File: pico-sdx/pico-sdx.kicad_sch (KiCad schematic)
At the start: 5 parts, among them J1 AudioJack3, J2 AudioJack3, J3 Screw_Terminal_01x02, J4 Conn_Coaxial, J5 Conn_Coaxial

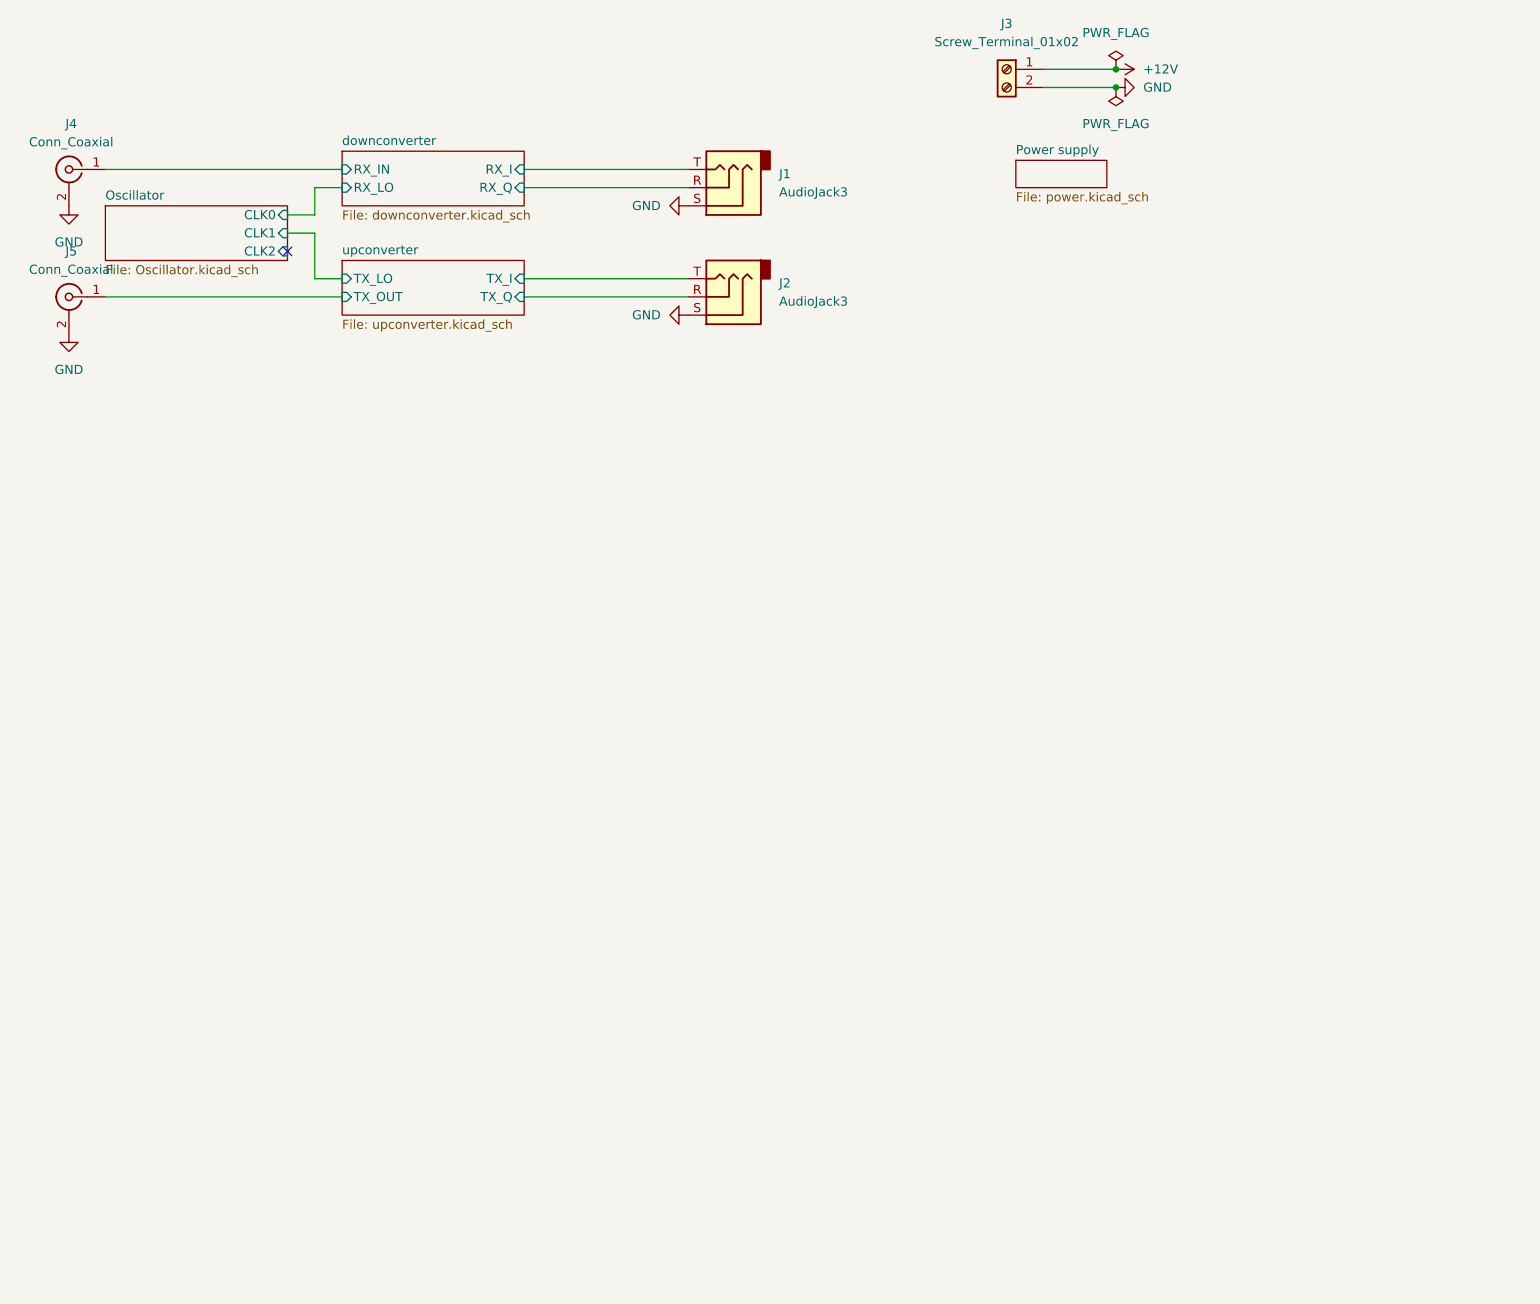
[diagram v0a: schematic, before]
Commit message: add documentation and RaspberryPi Pico
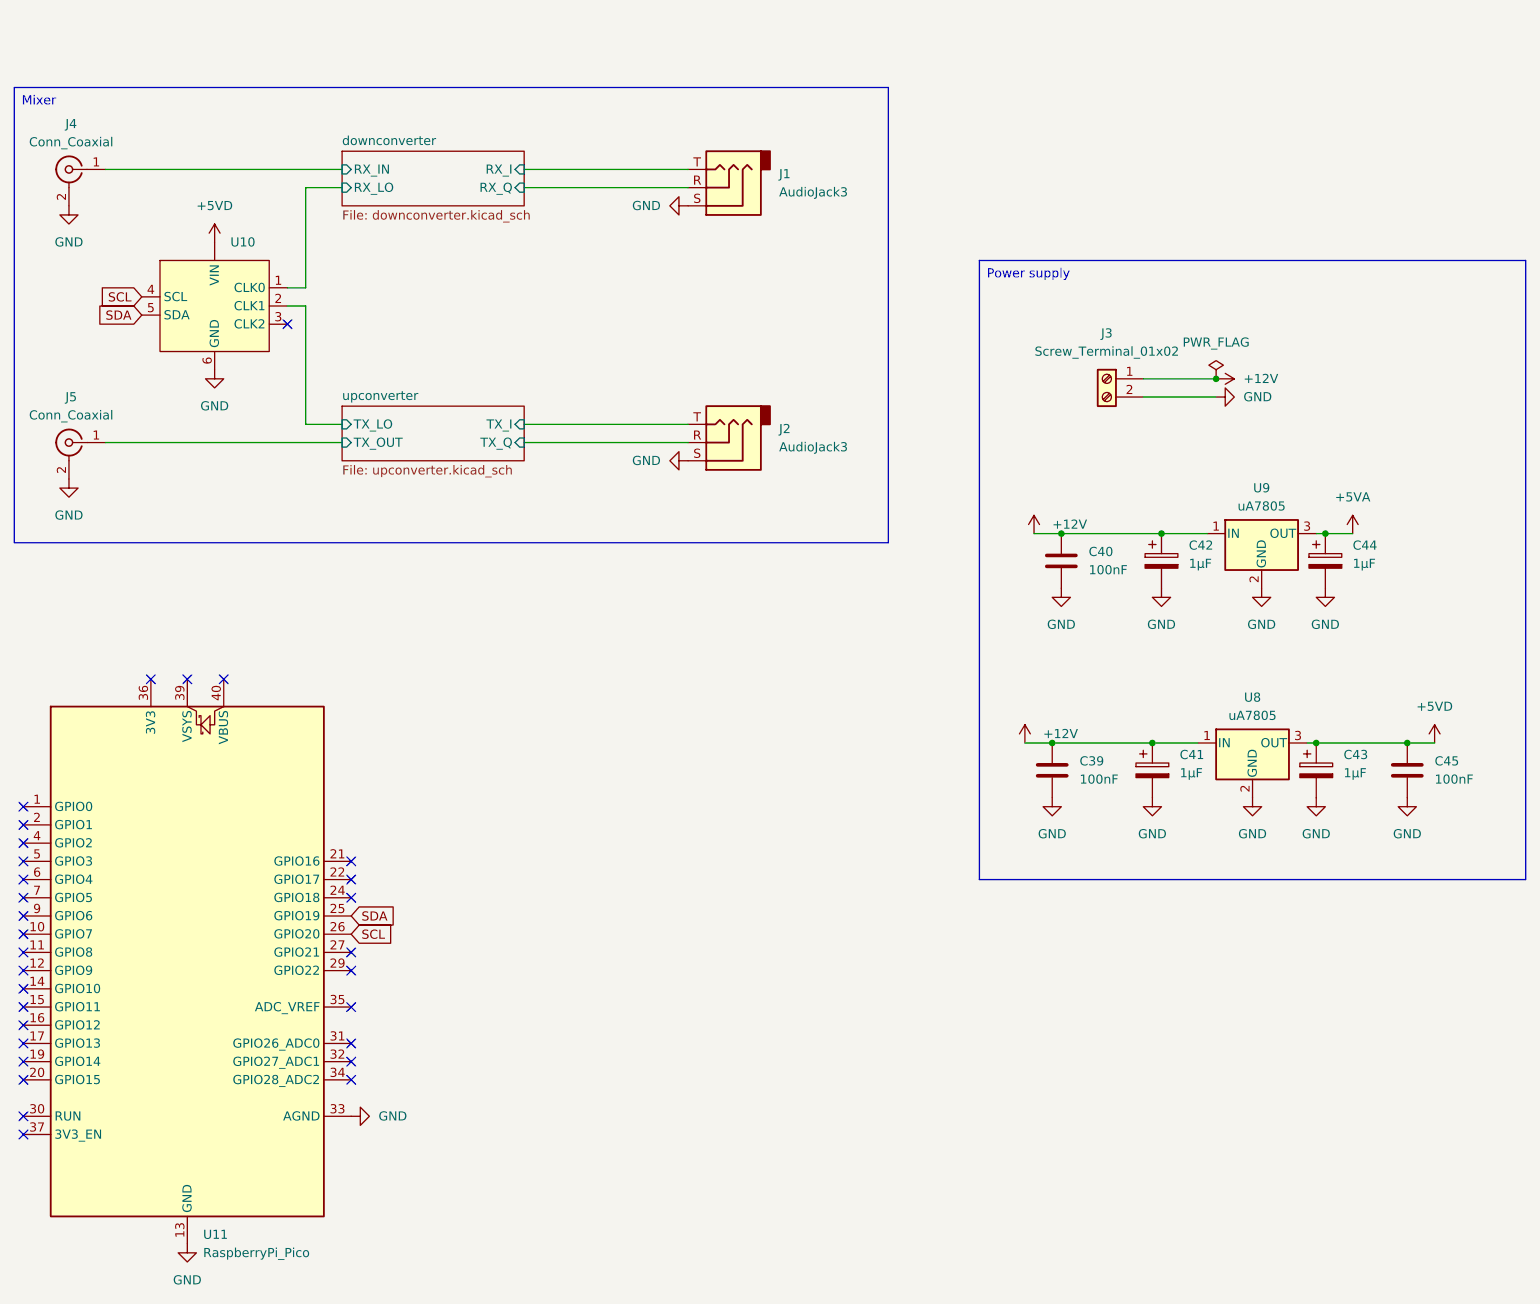
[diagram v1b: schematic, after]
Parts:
- added C39, C40, C45: 100nF, Capacitor_SMD:C_0603_1608Metric, symbol Device:C
- added C41, C42, C43, C44: 1µF, Capacitor_Tantalum_SMD:CP_EIA-3216-18_Kemet-A, symbol Device:C_Polarized
- added U10: ~, pico-sdx:Module_Si5351, symbol pico-sdx:Si5351A_Clock_Generator_Breakout_
- added U11: RaspberryPi_Pico, Module_RaspberryPi_Pico:RaspberryPi_Pico_Common, symbol MCU_Module_RaspberryPi_Pico:RaspberryPi_Pico
- added U8, U9: uA7805, Package_TO_SOT_THT:TO-220-3_Vertical, symbol Regulator_Linear:uA7805
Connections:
- net +12V: now also C39.1, C40.1, C41.1, C42.1, U8.1 (IN), U9.1 (IN)
- net GND: now also C39.2, C40.2, C41.2, C42.2, C43.2, C44.2, C45.2, U10.6 (GND), U11.13 (GND), U11.18 (GND), U11.23 (GND), U11.28 (GND), U11.3 (GND), U11.33 (AGND), U11.38 (GND), U11.8 (GND), U8.2 (GND), U9.2 (GND)
- new net +5VA: C44.1, U9.3 (OUT)
- new net +5VD: C43.1, C45.1, U10. (VIN), U8.3 (OUT)
- new net SCL: U10.4 (SCL), U11.26 (GPIO20)
- new net SDA: U10.5 (SDA), U11.25 (GPIO19)
- new net downconverter/RX_LO: U10.1 (CLK0)
- new net upconverter/TX_LO: U10.2 (CLK1)
- no-connect marks 1 -> 31
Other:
- removed sheet Oscillator
- removed sheet Power supply
- moved on the sheet: J2, J3, J5

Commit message: routed with filter relays without PA
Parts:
- removed J3: Screw_Terminal_01x02, TerminalBlock:TerminalBlock_Wuerth_691311400102_P7.62mm, symbol Connector:Screw_Terminal_01x02
- added D1, D2: D, Diode_SMD:D_SOD-128, symbol Device:D
- added J1: Antenna, Connector_Coaxial:SMA_Amphenol_132289_EdgeMount, symbol Connector:Conn_Coaxial
- added J2: RX, Connector_Coaxial:SMA_Amphenol_132289_EdgeMount, symbol Connector:Conn_Coaxial
- added J3: TX, Connector_Coaxial:SMA_Amphenol_132289_EdgeMount, symbol Connector:Conn_Coaxial
- added J8: Barrel_Jack_Switch, Connector_BarrelJack:BarrelJack_Wuerth_6941xx301002, symbol Connector:Barrel_Jack_Switch
- added K1, K2: G6K-2, Relay_THT:Relay_DPDT_Omron_G6K-2P, symbol Relay:G6K-2
- added TP1: RX_LO, TestPoint:TestPoint_Loop_D1.80mm_Drill1.0mm_Beaded, symbol Connector:TestPoint
- added TP2: TX_LO, TestPoint:TestPoint_Loop_D1.80mm_Drill1.0mm_Beaded, symbol Connector:TestPoint
- added U1: MAX4820xUP, Package_SO:HTSSOP-20-1EP_4.4x6.5mm_P0.65mm_EP2.85x4mm, symbol Driver_Relay:MAX4820xUP
- J4, J5: footprint Connector_Coaxial:SMA_Amphenol_132289_EdgeMount -> Connector_Coaxial:SMA_Amphenol_132291_Vertical
- renumbered C39 to C1, C40 to C2, C41 to C3, C42 to C4, C43 to C5, C44 to C6, C45 to C7, J1 to J6, J2 to J7, U11 to U2, U10 to U3, U8 to U4, U9 to U5
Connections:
- net Downconverter/RX_LO is gone; now on net +5VD: U3.1 (VIN)
- net Upconverter/TX_LO is gone; now on net GND: U3.2 (GND)
- net +12V: now also J8.1
- net +5VD: now also U2.39 (VSYS), U1.1 (VCC), U1.15 (COM), U1.2 (~{SET}); no longer U3. (VIN)
- net GND: now also D1.2 (A), D2.2 (A), J1.2 (Ext), J2.2 (Ext), J3.2 (Ext), J8.2, K1.8, K2.8, U1.12 (GND), U1.18 (GND), U1.21 (GND), U1.9 (GND); no longer U3.6 (GND)
- net SCL: now also U2.20 (GPIO15); no longer U2.26 (GPIO20)
- net SDA: now also U2.19 (GPIO14), U3.3 (SDA); no longer U2.25 (GPIO19), U3.5 (SDA)
- net Downconverter/RX_IN: now also K1.2
- net Upconverter/TX_OUT: now also K1.5
- net MISO: now reaches U2.21 (GPIO16)
- net MISO: now also U1.7 (DOUT)
- net ~{CS}: now reaches U2.22 (GPIO17)
- net ~{CS}: now also U1.4 (~{CS})
- net SCLK: now reaches U2.24 (GPIO18)
- net SCLK: now also U1.6 (SCLK)
- new net: J2.1 (In), K1.7, K2.2
- new net: J1.1 (In), K2.3
- new net 10 m: U1.20 (OUT1)
- new net 12 m: U1.19 (OUT2)
- new net 15 m: U1.17 (OUT3)
- new net 17 m: U1.16 (OUT4)
- new net 20 m: U1.14 (OUT5)
- new net 30 m: U1.13 (OUT6)
- new net 40 m: U1.11 (OUT7)
- new net Bandpass Filter/RF in: K1.6
- new net Buffer Amplifier/RF out: K1.3
- new net MOSI: U1.5 (DIN), U2.25 (GPIO19)
- new net PA/TX in: J3.1 (In), K1.4
- new net PA/TX out: K2.4
- new net RX_LO: TP1.1, U3.6 (CLK1)
- new net TX_LO: TP2.1, U3.7 (CLK0)
- new net TX~{RX}: D1.1 (K), D2.1 (K), K1.1, K2.1, U1.10 (OUT8)
- new net ~{RESET}: U1.3 (~{RESET}), U2.26 (GPIO20)
- no-connect marks 31 -> 29
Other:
- sheet downconverter renamed Downconverter
- sheet upconverter renamed Upconverter
- added sheet Bandpass Filter (bpf.kicad_sch)
- added sheet Buffer Amplifier (buffer.kicad_sch)
- added sheet PA (PA.kicad_sch)
- moved on the sheet: J4, J5

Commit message: modular design
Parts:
- removed D1, D2: D, Diode_SMD:D_SOD-128, symbol Device:D
- removed J1: Antenna, Connector_Coaxial:SMA_Amphenol_132289_EdgeMount, symbol Connector:Conn_Coaxial
- removed J2: RX, Connector_Coaxial:SMA_Amphenol_132289_EdgeMount, symbol Connector:Conn_Coaxial
- removed J3: TX, Connector_Coaxial:SMA_Amphenol_132289_EdgeMount, symbol Connector:Conn_Coaxial
- removed K1, K2: G6K-2, Relay_THT:Relay_DPDT_Omron_G6K-2P, symbol Relay:G6K-2
- removed TP1: RX_LO, TestPoint:TestPoint_Loop_D1.80mm_Drill1.0mm_Beaded, symbol Connector:TestPoint
- removed TP2: TX_LO, TestPoint:TestPoint_Loop_D1.80mm_Drill1.0mm_Beaded, symbol Connector:TestPoint
- removed U1: MAX4820xUP, Package_SO:HTSSOP-20-1EP_4.4x6.5mm_P0.65mm_EP2.85x4mm, symbol Driver_Relay:MAX4820xUP
- removed U2: RaspberryPi_Pico, Module_RaspberryPi_Pico:RaspberryPi_Pico_Common, symbol MCU_Module_RaspberryPi_Pico:RaspberryPi_Pico
- removed U3: ~, pico-sdx:Module_Si5351, symbol pico-sdx:Si5351A_Clock_Generator_Breakout_
- removed U4: uA7805, Package_TO_SOT_THT:TO-220-3_Vertical, symbol Regulator_Linear:uA7805
- added PMOD1: PMOD-Device-x2-Type-2A-Expanded-SPI, pmod-conn_6x2:pmod_pin_array_6x2, symbol pmod:PMOD-Device-x2-Type-2A-Expanded-SPI
- added U17: TLE4284 DV33, Package_TO_SOT_SMD:TO-252-3_TabPin2, symbol Regulator_Linear:AMS1117CD-3.3
- added U3: Si5351C-B-GU, Package_SO:QSOP-24_3.9x8.7mm_P0.635mm, symbol pico-sdx:Si5351C-B-GU
- added X8: TCXO-14, Oscillator:Oscillator_DIP-14, symbol Oscillator:TCXO-14
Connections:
- net +12V: now also U17.3 (VI)
- net GND: now also U17.1 (GND), U3.13 (OEB), U3.17 (GND), U3.19 (GND), U3.5 (GND), U3.8 (GND), X8.7 (GND)
- net RX_LO: now also U3.21 (CLK0)
- net SCL: now also U3.10 (SCL)
- net SDA: now also U3.22 (VDDOD)
- net TX_LO: now also U3.20 (CLK1)
- net +5VD renamed +3.3V
- net +3.3V: now also U17.2 (VO), U3.16 (VDDOB), U3.18 (VDDOA), U3.2 (VDDOC), U3.22 (VDDOD), U3.4 (VDD), X8.14 (Vcc)
- net Downconverter/RX_IN renamed Buffer Amplifier/RF in
- new net: U3.12 (CLKIN), X8.8 (OUT)
- no-connect marks 29 -> 10
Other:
- removed sheet Bandpass Filter
- removed sheet PA
- moved on the sheet: J4, J5

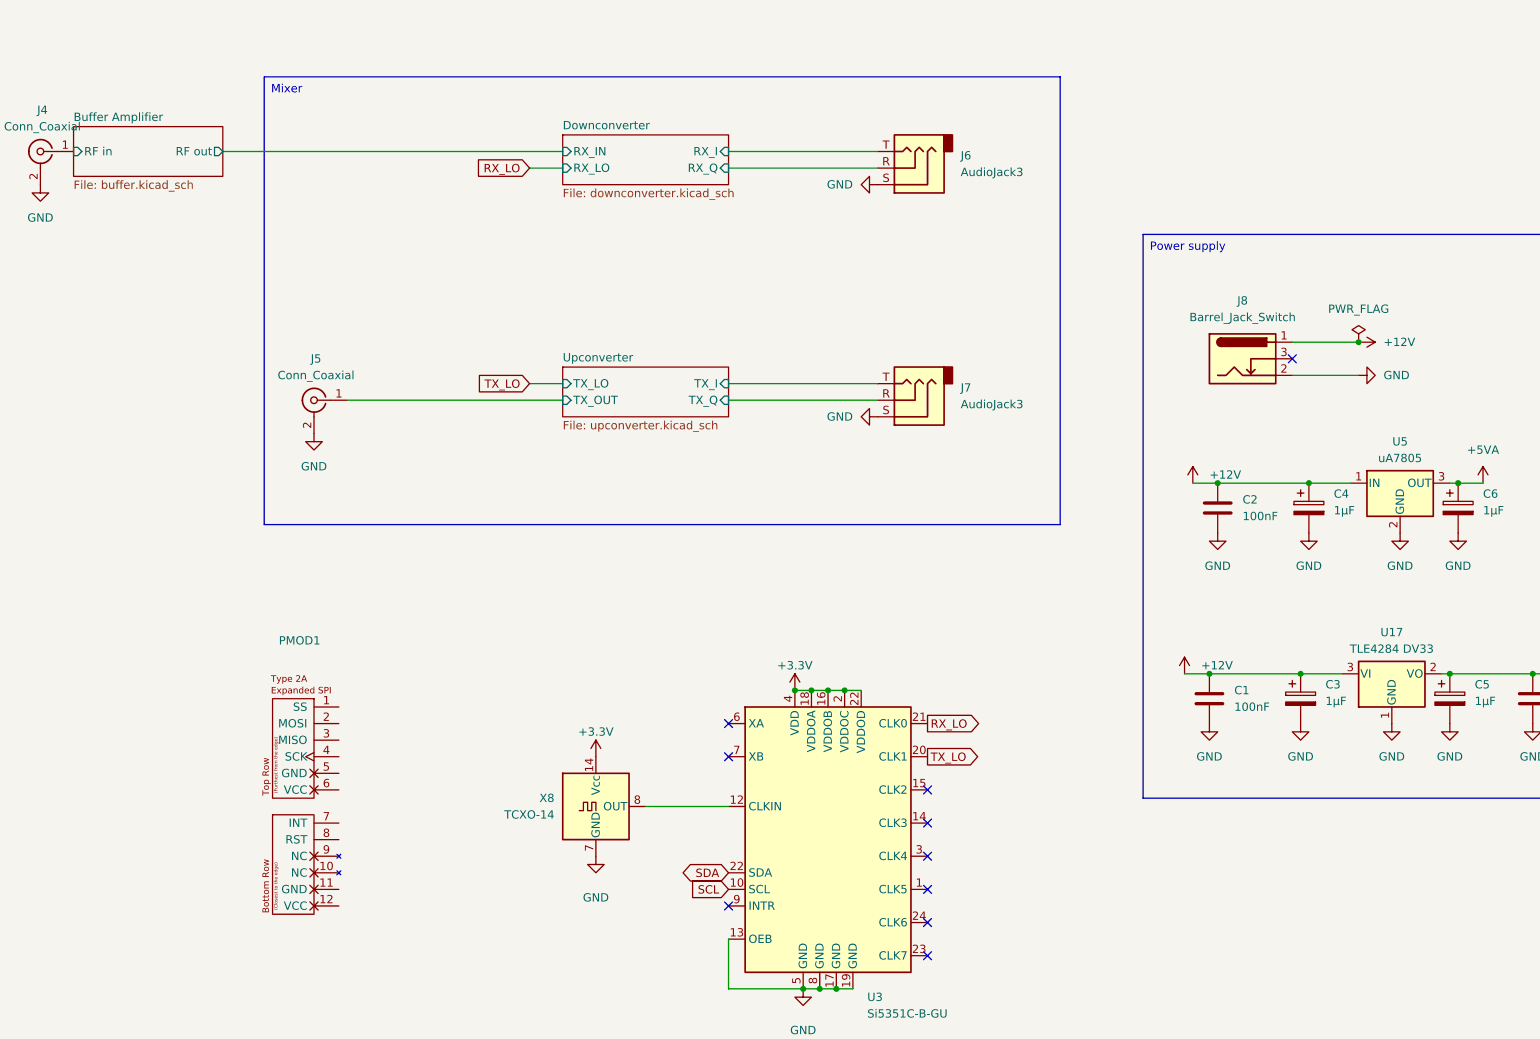
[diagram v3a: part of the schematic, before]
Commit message: mixer routed
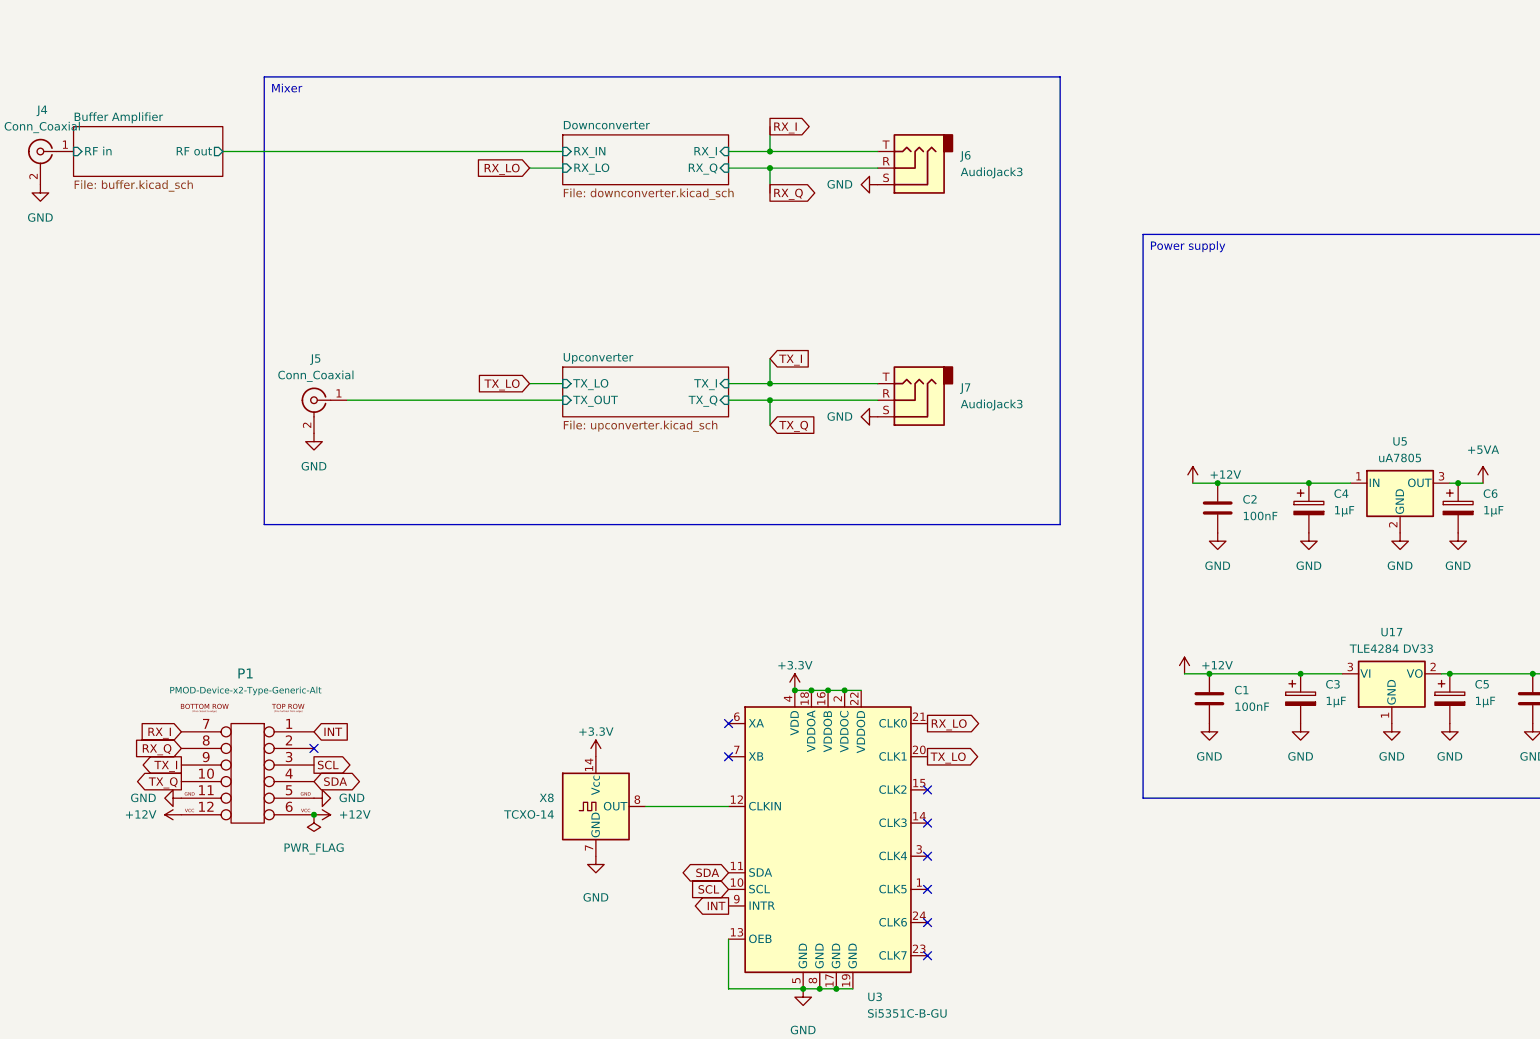
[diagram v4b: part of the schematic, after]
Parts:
- removed J8: Barrel_Jack_Switch, Connector_BarrelJack:BarrelJack_Wuerth_6941xx301002, symbol Connector:Barrel_Jack_Switch
- removed PMOD1: PMOD-Device-x2-Type-2A-Expanded-SPI, pmod-conn_6x2:pmod_pin_array_6x2, symbol pmod:PMOD-Device-x2-Type-2A-Expanded-SPI
- added P1: PMOD-Device-x2-Type-Generic-Alt, pmod-conn_6x2:pmod_pin_array_6x2, symbol pmod:PMOD-Device-x2-Type-Generic-Alt
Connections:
- net +12V: now also P1.12 (P12), P1.6 (P6)
- net GND: now also P1.11 (P11), P1.5 (P5)
- net SCL: now also P1.3 (P3)
- net SDA: now also U3.11 (SDA), P1.4 (P4); no longer U3.22 (VDDOD)
- net INT: now reaches U3.9 (INTR)
- net INT: now also P1.1 (P1)
- net Downconverter/RX_I renamed RX_I
- net RX_I: now also P1.7 (P7)
- net Downconverter/RX_Q renamed RX_Q
- net RX_Q: now also P1.8 (P8)
- net Upconverter/TX_I renamed TX_I
- net TX_I: now also P1.9 (P9)
- net Upconverter/TX_Q renamed TX_Q
- net TX_Q: now also P1.10 (P10)
- no-connect marks 10 -> 9
